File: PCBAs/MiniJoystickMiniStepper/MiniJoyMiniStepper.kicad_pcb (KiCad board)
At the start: 2 copper layers, 88.9 x 142.2 mm, 94 parts, among them J0 STEPPER_UNI_5P, J1 STEPPER_UNI_5P, J10 TH_0.1_1x1, J100 TH_0.1_1x1, J101 TH_0.1_1x1, J102 TH_0.1_1x1, J103 TH_0.1_1x1, J104 TH_0.1_1x1, J105 TH_0.1_1x1, J107 TH_0.1_1x1, J11 TH_0.1_1x1, J12 TH_0.1_1x1, J13 TH_0.1_1x1, J14 TH_0.1_1x1, J15 TH_0.1_1x1, J16 TH_0.1_1x1, J2 STEPPER_UNI_5P, J3 STEPPER_UNI_5P, J4 STEPPER_UNI_5P, J5 STEPPER_UNI_5P, J6 STEPPER_UNI_5P, J7 STEPPER_UNI_5P, J8 TH_0.1_1x1, J9 TH_0.1_1x1, U1 MCP3008T-I/SL, U10 ULN2803, U11 STM32F103C8T6_BLUE_PILL, U2 OLED_128x32_I2C, U3 CD74HC595, U4 CD74HC595, U5 CD74HC595, U6 CD74HC595, U7 ULN2803, U8 ULN2803, U9 ULN2803

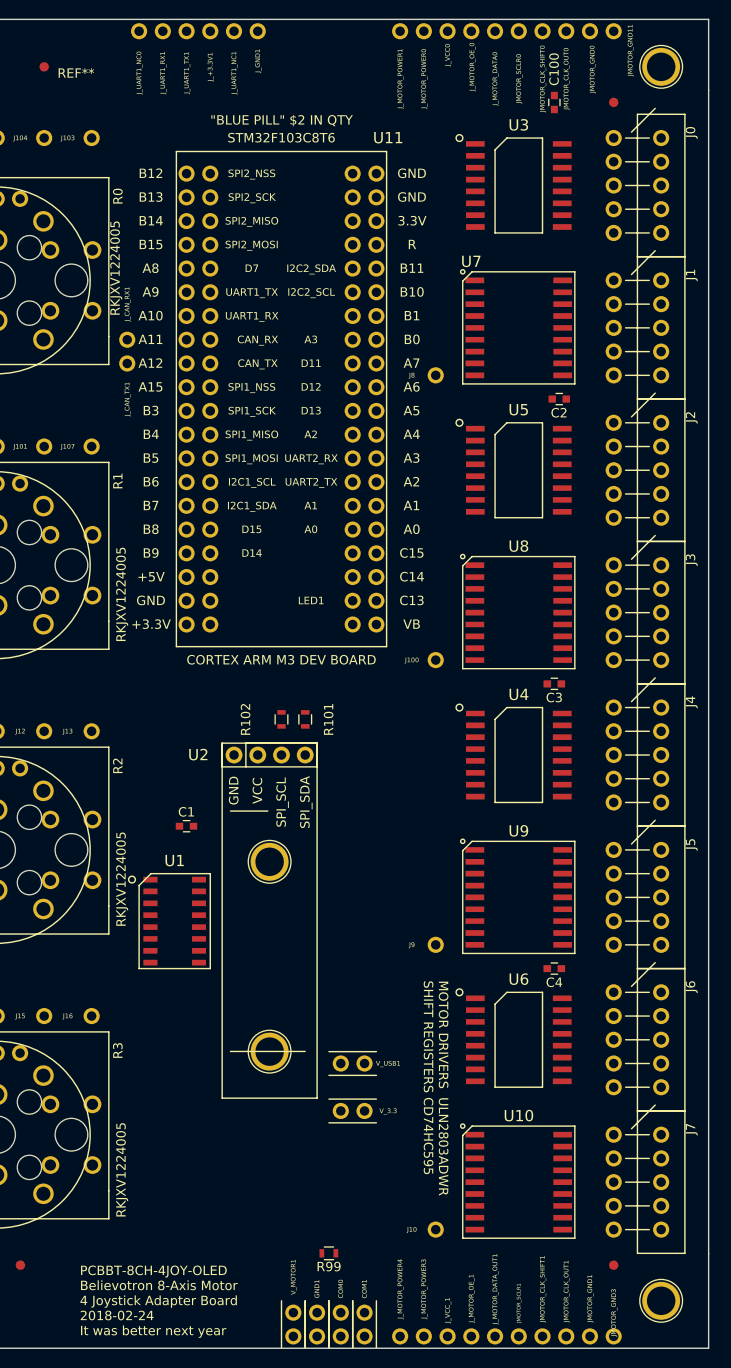
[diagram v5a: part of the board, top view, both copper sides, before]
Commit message: Updated PCB silkscreen. Added design sugar, part numbers, part function, better labeling
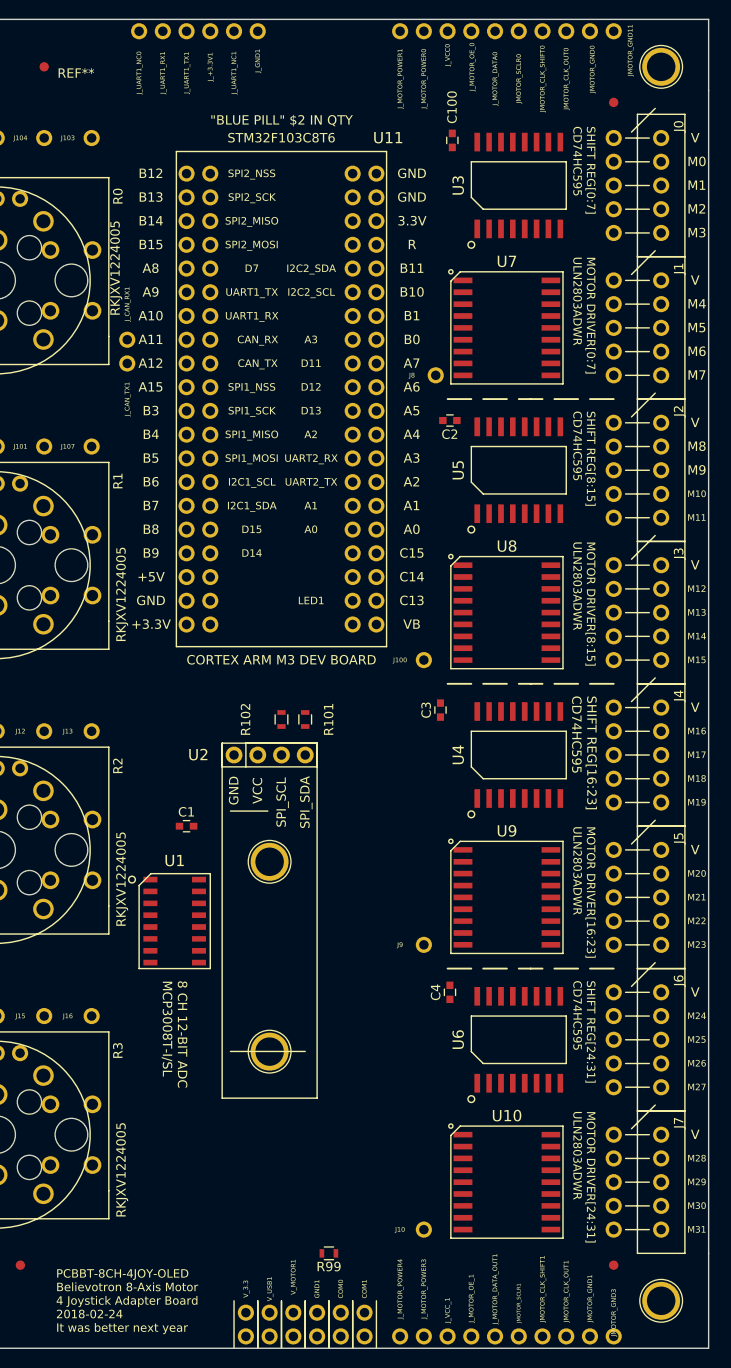
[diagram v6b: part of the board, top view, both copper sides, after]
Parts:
- moved V_USB1 28.5 mm to (143.5, 156.2), turned to 270 degrees
- moved V_3.3 25.0 mm to (141.0, 156.2), turned to 270 degrees
- moved C3 12.5 mm to (161.8, 91.7), turned to 90 degrees
- moved C2 11.9 mm to (162.8, 60.7)
- moved C100 11.7 mm to (163.1, 30.7)
- moved C4 11.5 mm to (162.8, 121.9), turned to 90 degrees
- moved U10 1.27 mm to (168.9, 142.2)
- moved U7 1.27 mm to (168.9, 50.8)
- moved U8 1.27 mm to (168.9, 81.3)
- moved U9 1.27 mm to (168.9, 111.8)
- moved J10 1.27 mm to (160.0, 147.3)
- moved J100 1.27 mm to (160.0, 86.4)
- moved J9 1.27 mm to (160.0, 116.8)
- turned U3 to 0 degrees
- turned U4 to 0 degrees
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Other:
- board text added: "8 CH 12-BIT ADC MCP3008T-I/SL"
- board text added: "M0"
- board text added: "M1"
- board text added: "M10"
- board text added: "M11"
- board text added: "M12"
- board text added: "M13"
- board text added: "M14"
- board text added: "M15"
- board text added: "M16"
- board text added: "M17"
- board text added: "M18"
- board text added: "M19"
- board text added: "M2"
- board text added: "M20"
- board text added: "M21"
- board text added: "M22"
- board text added: "M23"
- board text added: "M24"
- board text added: "M25"
- board text added: "M26"
- board text added: "M27"
- board text added: "M28"
- board text added: "M29"
- board text added: "M3"
- board text added: "M30"
- board text added: "M31"
- board text added: "M4"
- board text added: "M5"
- board text added: "M6"
- board text added: "M7"
- board text added: "M8"
- board text added: "M9"
- board text added: "MOTOR DRIVER[0:7] ULN2803ADWR"
- board text added: "MOTOR DRIVER[16:23] ULN2803ADWR"
- board text added: "MOTOR DRIVER[24:31] ULN2803ADWR"
- board text added: "MOTOR DRIVER[8:15] ULN2803ADWR"
- board text added: "SHIFT REG[0:7] CD74HC595"
- board text added: "SHIFT REG[16:23] CD74HC595"
- board text added: "SHIFT REG[24:31] CD74HC595"
- board text added: "SHIFT REG[8:15] CD74HC595"
- board text added: "V"
- board text removed: "MOTOR DRIVERS ULN2803ADWR SHIFT REGISTERS CD74HC595"

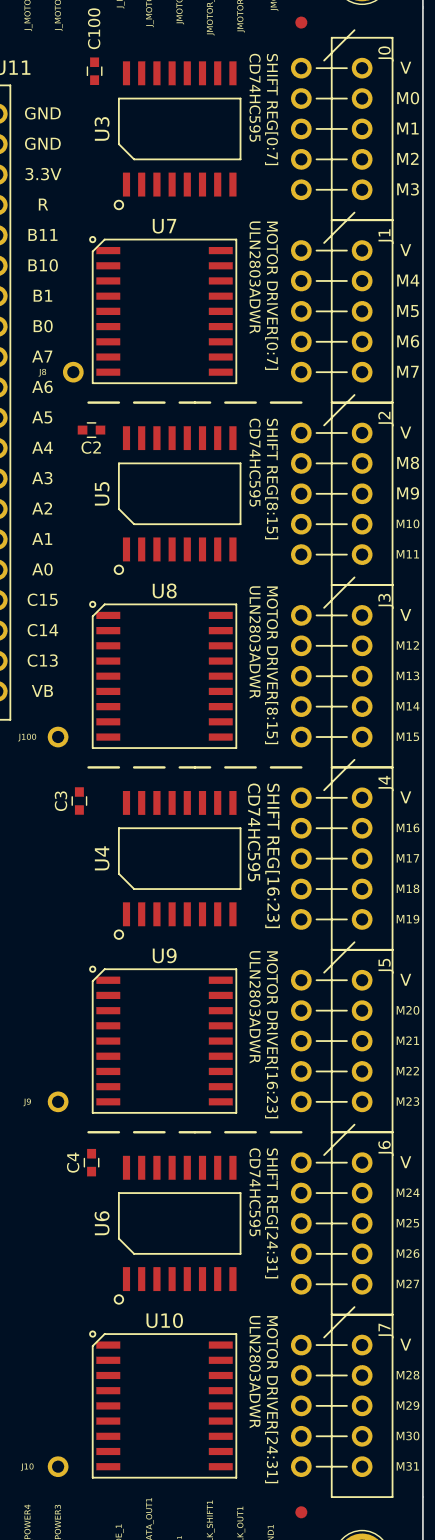
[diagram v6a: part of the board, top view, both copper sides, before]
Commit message: Fixed PCB bug: Reconnected pads to nets
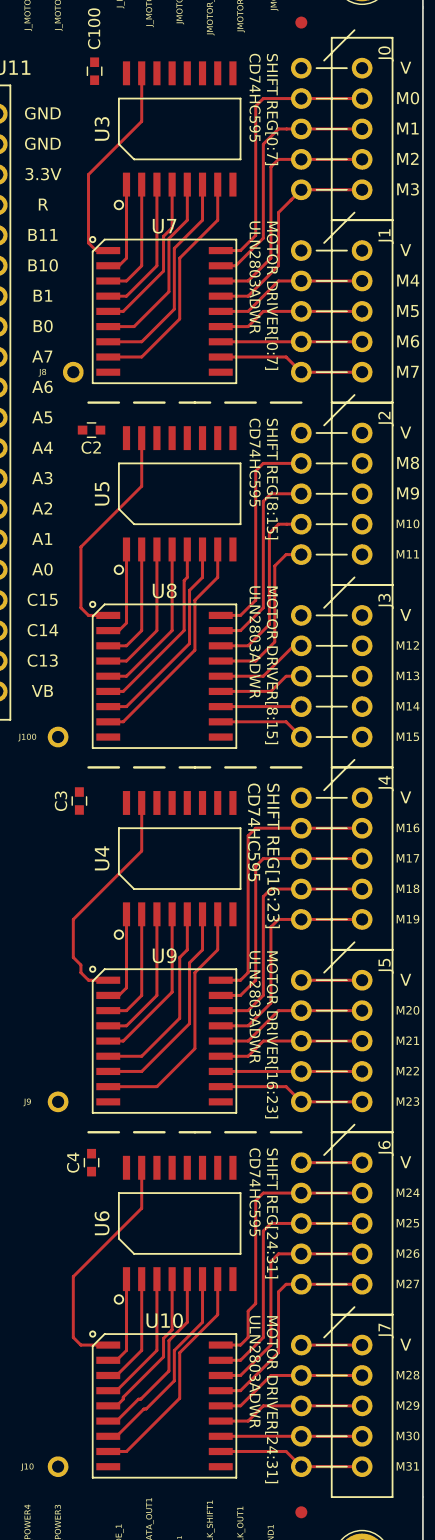
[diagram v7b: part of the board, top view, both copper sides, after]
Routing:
- net Net-(J4-Pad2): track 0.00 -> 23.8 mm
- net Net-(J6-Pad2): track 0.00 -> 23.4 mm
- net Net-(J0-Pad2): track 0.00 -> 23.4 mm
- net Net-(J4-Pad3): track 0.00 -> 22.1 mm
- net Net-(J6-Pad3): track 0.00 -> 21.8 mm
- net Net-(J0-Pad3): track 0.00 -> 21.1 mm
- net Net-(J4-Pad4): track 0.00 -> 20.9 mm
- net Net-(U4-Pad7): track 0.00 -> 20.6 mm
- net Net-(J0-Pad4): track 0.00 -> 20.5 mm
- net Net-(J6-Pad4): track 0.00 -> 20.1 mm
- net Net-(U3-Pad7): track 0.00 -> 19.8 mm
- net Net-(U10-Pad1): track 0.00 -> 19.7 mm
- net Net-(U4-Pad15): track 0.00 -> 19.4 mm
- net Net-(J4-Pad5): track 0.00 -> 19.2 mm
- net Net-(U10-Pad8): track 0.00 -> 19.1 mm
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
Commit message: Mid-route
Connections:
- JMOTOR_CLK_OUT0 pad 1: Net-(JMOTOR_CLK_OUT0-Pad1) -> /MOTOR_CLK_OUT
- JMOTOR_CLK_SHIFT0 pad 1: Net-(JMOTOR_CLK_SHIFT0-Pad1) -> /MOTOR_CLK_SHIFT
- JMOTOR_SCLR0 pad 1: Net-(JMOTOR_SCLR0-Pad1) -> /!MOTOR_SCLR
- J_MOTOR_DATA0 pad 1: Net-(J_MOTOR_DATA0-Pad1) -> /MOTOR_DATA
- J_MOTOR_OE_0 pad 1: Net-(J_MOTOR_OE_0-Pad1) -> /!MOTOR_OE
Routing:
- net /MOTOR_CLK_OUT: track 0.00 -> 195.1 mm, vias 0 -> 8
- net /MOTOR_CLK_SHIFT: track 0.00 -> 188.3 mm, vias 0 -> 9
- net /!MOTOR_OE: track 0.00 -> 180.7 mm, vias 0 -> 7
- net /!MOTOR_SCLR: track 0.00 -> 81.3 mm, vias 0 -> 5
- net /MOTOR_DATA: track 0.00 -> 66.5 mm, vias 0 -> 1
- net Net-(U3-Pad9): track 0.00 -> 34.1 mm
- net +3V3: track 0.00 -> 16.0 mm, vias 0 -> 1
